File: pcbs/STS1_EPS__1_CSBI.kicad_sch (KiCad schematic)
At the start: 2 parts

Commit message: worked on sts1_eps_1
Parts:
- added H1, H2, H3, H4: MountingHole, MountingHole:MountingHole_4.3mm_M4_Pad_Via, symbol Mechanical:MountingHole
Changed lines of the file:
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@@
     (pin "1")
+  )
+  (symbol (lib_id "Mechanical:MountingHole") (at 23.114 21.59 0) (unit 1)
+    (in_bom yes) (on_board yes) (fields_autoplaced)
+    (property "Reference" "H1" (id 0) (at 26.67 20.3199 0)
+      (effects (font (size 1.27 1.27)) (justify left))
+    )
+    (property "Value" "MountingHole" (id 1) (at 26.67 22.8599 0)
+      (effects (font (size 1.27 1.27)) (justify left))
+    )
+    (property "Footprint" "MountingHole:MountingHole_4.3mm_M4_Pad_Via" (id 2) (at 23.114 21.59 0)
+      (effects (font (size 1.27 1.27)) hide)
+    )
+    (property "Datasheet" "~" (id 3) (at 23.114 21.59 0)
+      (effects (font (size 1.27 1.27)) hide)
+    )
+  )
+  (symbol (lib_id "Mechanical:MountingHole") (at 23.114 32.258 0) (unit 1)
+    (in_bom yes) (on_board yes) (fields_autoplaced)
+    (property "Reference" "H3" (id 0) (at 26.67 30.9879 0)
+      (effects (font (size 1.27 1.27)) (justify left))
+    )
+    (property "Value" "MountingHole" (id 1) (at 26.67 33.5279 0)
+      (effects (font (size 1.27 1.27)) (justify left))
+    )
+    (property "Footprint" "MountingHole:MountingHole_4.3mm_M4_Pad_Via" (id 2) (at 23.114 32.258 0)
+      (effects (font (size 1.27 1.27)) hide)
+    )
+    (property "Datasheet" "~" (id 3) (at 23.114 32.258 0)
+      (effects (font (size 1.27 1.27)) hide)
+    )
+  )
+  (symbol (lib_id "Mechanical:MountingHole") (at 23.114 37.338 0) (unit 1)
+    (in_bom yes) (on_board yes) (fields_autoplaced)
+    (property "Reference" "H4" (id 0) (at 26.67 36.0679 0)
+      (effects (font (size 1.27 1.27)) (justify left))
+    )
+    (property "Value" "MountingHole" (id 1) (at 26.67 38.6079 0)
+      (effects (font (size 1.27 1.27)) (justify left))
+    )
+    (property "Footprint" "MountingHole:MountingHole_4.3mm_M4_Pad_Via" (id 2) (at 23.114 37.338 0)
+      (effects (font (size 1.27 1.27)) hide)
+    )
+    (property "Datasheet" "~" (id 3) (at 23.114 37.338 0)
+      (effects (font (size 1.27 1.27)) hide)
+    )
+  )
+  (symbol (lib_id "Mechanical:MountingHole") (at 23.114 26.924 0) (unit 1)
+    (in_bom yes) (on_board yes) (fields_autoplaced)
+    (property "Reference" "H2" (id 0) (at 26.67 25.6539 0)
+      (effects (font (size 1.27 1.27)) (justify left))
+    )
+    (property "Value" "MountingHole" (id 1) (at 26.67 28.1939 0)
+      (effects (font (size 1.27 1.27)) (justify left))
+    )
+    (property "Footprint" "MountingHole:MountingHole_4.3mm_M4_Pad_Via" (id 2) (at 23.114 26.924 0)
+      (effects (font (size 1.27 1.27)) hide)
+    )
+    (property "Datasheet" "~" (id 3) (at 23.114 26.924 0)
+      (effects (font (size 1.27 1.27)) hide)
+    )
   )
   (sheet_instances

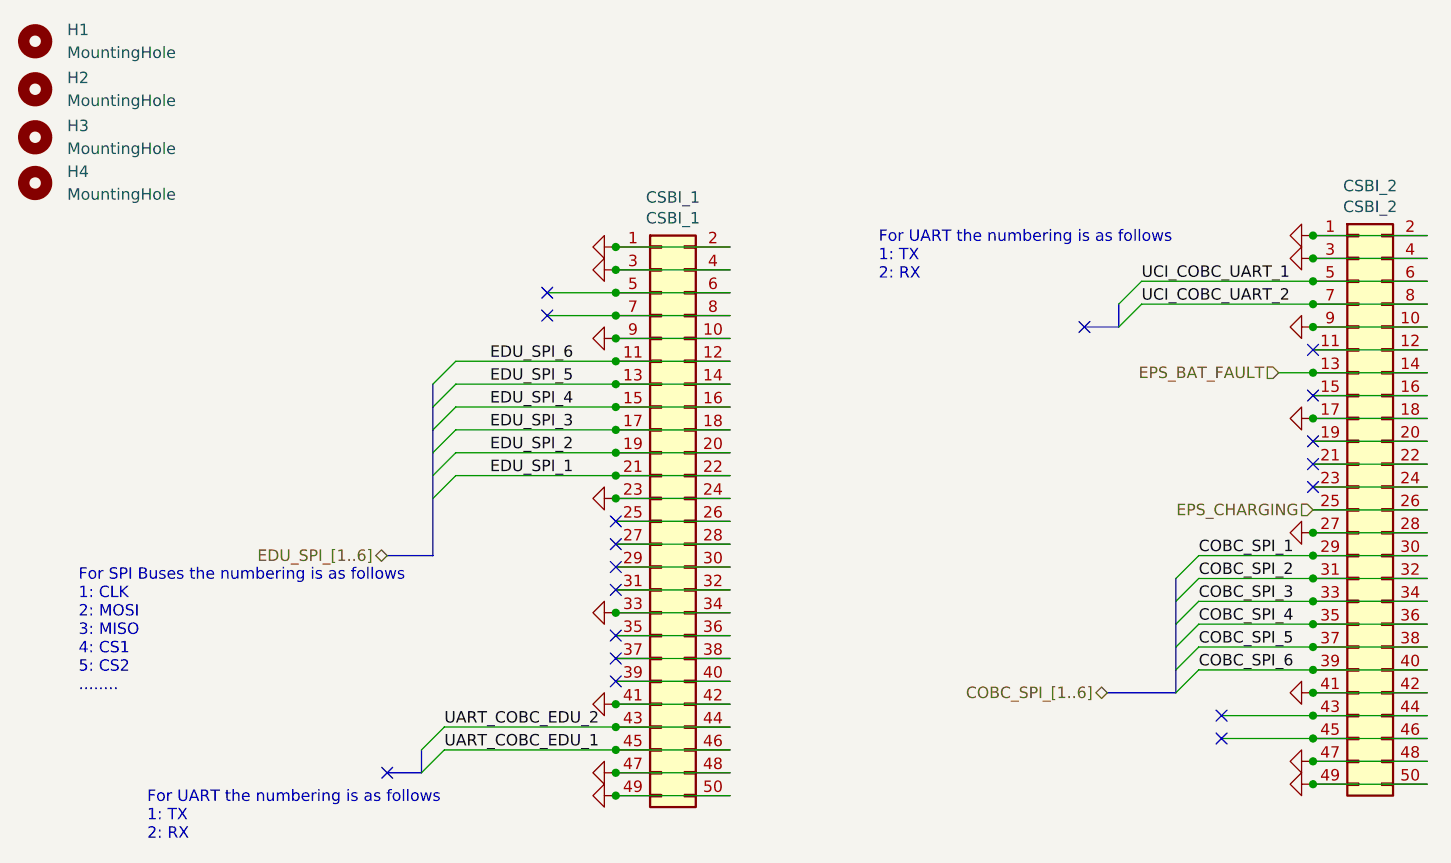
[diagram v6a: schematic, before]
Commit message: Worked on STS1_EPS_1.
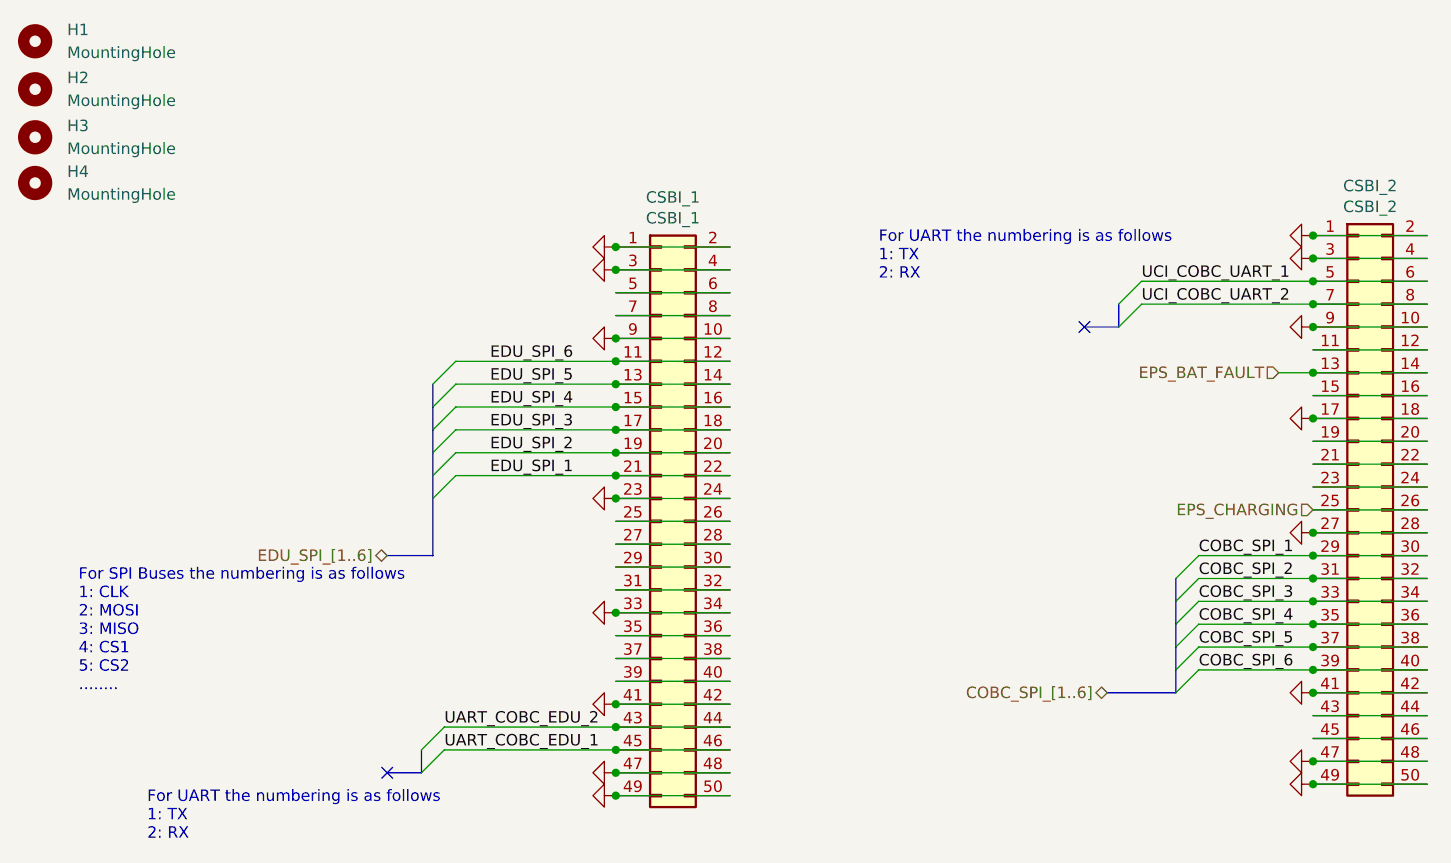
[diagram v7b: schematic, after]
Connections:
- no-connect marks 18 -> 2
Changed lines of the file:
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@@
   (junction (at 87.63 100.33) (diameter 0) (color 0 0 0 0)
   )
-  (junction (at 87.63 49.53) (diameter 0) (color 0 0 0 0)
-  )
   (junction (at 165.1 78.74) (diameter 0) (color 0 0 0 0)
   )
@@
   (junction (at 87.63 102.87) (diameter 0) (color 0 0 0 0)
   )
-  (junction (at 87.63 52.07) (diameter 0) (color 0 0 0 0)
-  )
   (junction (at 87.63 97.79) (diameter 0) (color 0 0 0 0)
   )
@@
   (junction (at 87.63 85.09) (diameter 0) (color 0 0 0 0)
   )
-  (junction (at 165.1 99.06) (diameter 0) (color 0 0 0 0)
-  )
   (junction (at 165.1 88.9) (diameter 0) (color 0 0 0 0)
   )
@@
   (junction (at 87.63 54.61) (diameter 0) (color 0 0 0 0)
   )
-  (junction (at 165.1 96.52) (diameter 0) (color 0 0 0 0)
-  )
   (junction (at 165.1 43.18) (diameter 0) (color 0 0 0 0)
   )
@@
   (junction (at 165.1 86.36) (diameter 0) (color 0 0 0 0)
   )
-  (no_connect (at 87.63 80.01))
-  (no_connect (at 87.63 77.47))
-  (no_connect (at 165.1 68.58))
-  (no_connect (at 165.1 55.88))
-  (no_connect (at 80.01 52.07))
-  (no_connect (at 87.63 74.93))
-  (no_connect (at 154.94 99.06))
-  (no_connect (at 87.63 82.55))
-  (no_connect (at 165.1 60.96))
-  (no_connect (at 165.1 66.04))
   (no_connect (at 62.23 102.87))
-  (no_connect (at 87.63 92.71))
-  (no_connect (at 87.63 90.17))
-  (no_connect (at 87.63 87.63))
   (no_connect (at 139.7 53.34))
-  (no_connect (at 154.94 96.52))
-  (no_connect (at 165.1 71.12))
-  (no_connect (at 80.01 49.53))
   (bus_entry (at 149.86 93.98) (size 2.54 -2.54)
     (stroke (width 0) (type default) (color 0 0 0 0))
@@
     (stroke (width 0) (type default) (color 0 0 0 0))
   )
-  (wire (pts (xy 154.94 96.52) (xy 165.1 96.52))
-    (stroke (width 0) (type default) (color 0 0 0 0))
-  )
   (wire (pts (xy 87.63 59.69) (xy 100.33 59.69))
     (stroke (width 0) (type default) (color 0 0 0 0))
   )
+  (wire (pts (xy 87.63 82.55) (xy 100.33 82.55))
+    (stroke (width 0) (type default) (color 0 0 0 0))
+  )
   (bus (pts (xy 143.51 53.34) (xy 139.7 53.34))
     (stroke (width 0) (type default) (color 0 0 0 0))
@@
     (stroke (width 0) (type default) (color 0 0 0 0))
   )
-  (wire (pts (xy 154.94 99.06) (xy 165.1 99.06))
-    (stroke (width 0) (type default) (color 0 0 0 0))
-  )
   (wire (pts (xy 165.1 99.06) (xy 177.8 99.06))
     (stroke (width 0) (type default) (color 0 0 0 0))
@@
     (stroke (width 0) (type default) (color 0 0 0 0))
   )
-  (wire (pts (xy 80.01 49.53) (xy 87.63 49.53))
-    (stroke (width 0) (type default) (color 0 0 0 0))
-  )
   (wire (pts (xy 165.1 81.28) (xy 152.4 81.28))
     (stroke (width 0) (type default) (color 0 0 0 0))
@@
     (stroke (width 0) (type default) (color 0 0 0 0))
   )
-  (wire (pts (xy 87.63 82.55) (xy 100.33 82.55))
-    (stroke (width 0) (type default) (color 0 0 0 0))
-  )
   (wire (pts (xy 165.1 93.98) (xy 177.8 93.98))
     (stroke (width 0) (type default) (color 0 0 0 0))
@@
     (stroke (width 0) (type default) (color 0 0 0 0))
   )
-  (wire (pts (xy 80.01 52.07) (xy 87.63 52.07))
-    (stroke (width 0) (type default) (color 0 0 0 0))
-  )
